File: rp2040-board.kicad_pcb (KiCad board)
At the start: 2 copper layers, 100.9 x 70.3 mm, 20 parts

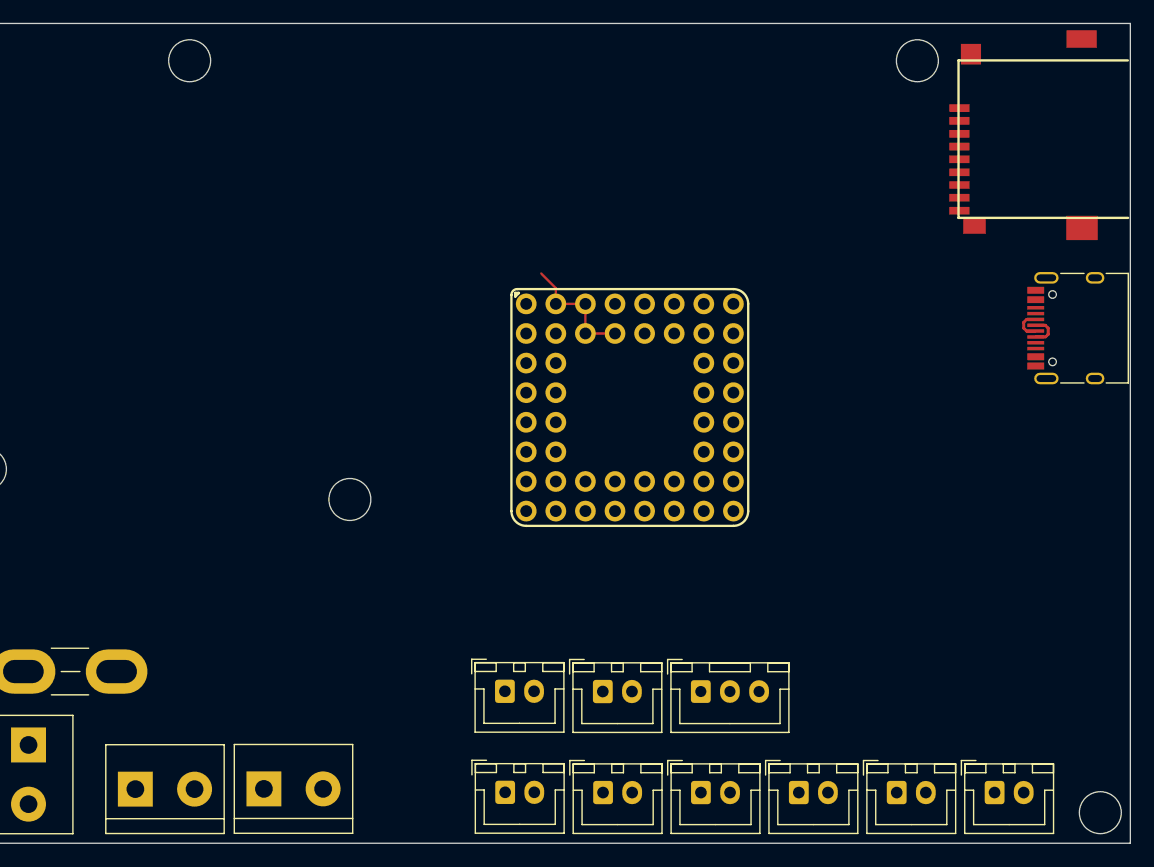
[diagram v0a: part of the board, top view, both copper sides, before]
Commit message: Minor Schematic Layout Changes
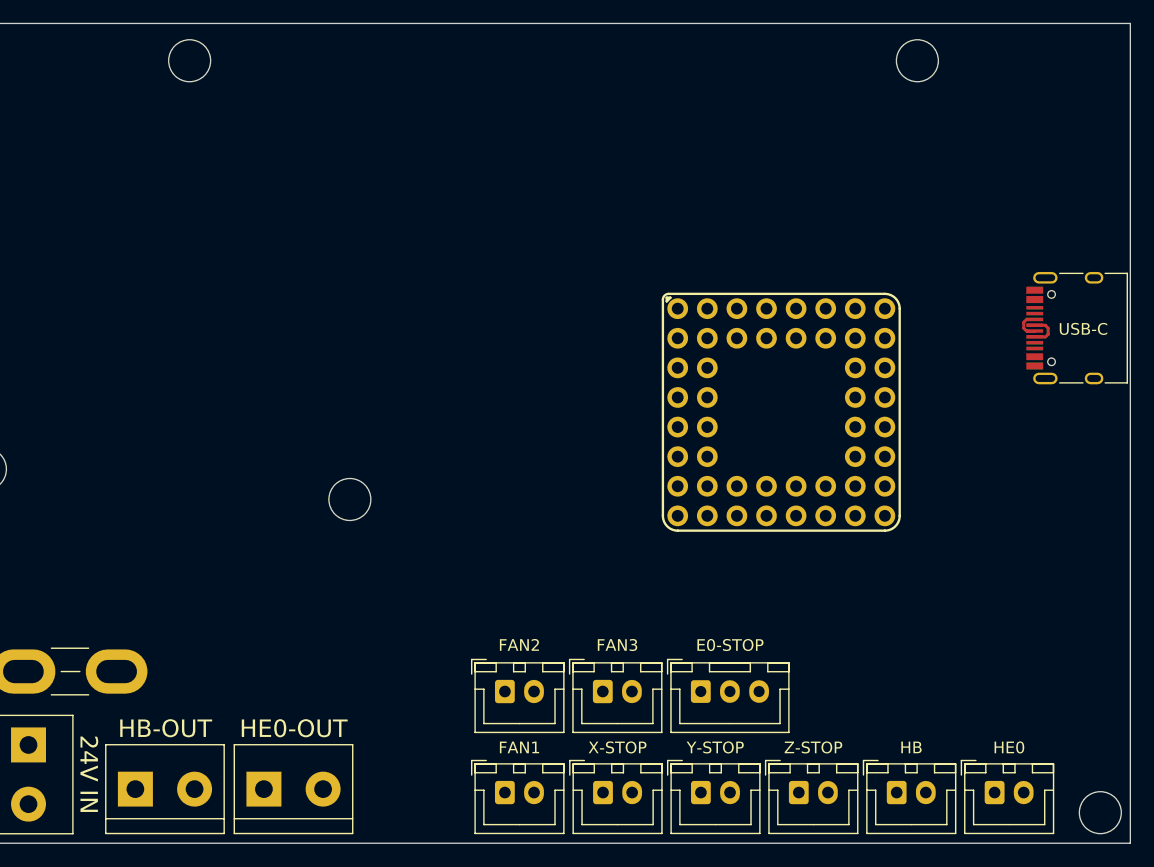
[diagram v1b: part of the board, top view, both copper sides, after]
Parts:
- moved REF** 13.0 mm to (173.0, 101.1)
- moved REF** 0.09 mm to (198.8, 93.9)
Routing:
- net (no net): track 16.4 -> 5.63 mm
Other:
- board text added: "24V IN"
- board text added: "E0-STOP"
- board text added: "FAN1"
- board text added: "FAN2"
- board text added: "FAN3"
- board text added: "HB"
- board text added: "HB-OUT"
- board text added: "HE0"
- board text added: "HE0-OUT"
- board text added: "USB-C"
- board text added: "X-STOP"
- board text added: "Y-STOP"
- board text added: "Z-STOP"

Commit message: Totally no 80% re-source of the BOM
suuurely no re-source
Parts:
- removed the REF** at (198.8, 93.9)
- added C11: 330uF, Capacitor_THT:CP_Radial_D8.0mm_P3.50mm, F.Cu at (109.1, 113.0)
- added C31: 100uF, Capacitor_THT:CP_Radial_D6.3mm_P2.50mm, F.Cu at (121.0, 79.0)
- added C32: 100uF, Capacitor_THT:CP_Radial_D6.3mm_P2.50mm, F.Cu at (141.7, 79.0)
- added C45: 100uF, Capacitor_THT:CP_Radial_D6.3mm_P2.50mm, F.Cu at (162.5, 79.0)
- added C46: 100uF, Capacitor_THT:CP_Radial_D6.3mm_P2.50mm, F.Cu at (183.5, 79.0)
- added J17: X-STEPPER, Connector_JST:JST_XH_B4B-XH-A_1x04_P2.50mm_Vertical, F.Cu at (116.3, 71.9)
- added J18: Y-STEPPER, Connector_JST:JST_XH_B4B-XH-A_1x04_P2.50mm_Vertical, F.Cu at (135.6, 71.9)
- added J19: ZA-STEPPER, Connector_JST:JST_XH_B4B-XH-A_1x04_P2.50mm_Vertical, F.Cu at (150.0, 71.9)
- added J2: USB4105-GF-A, ul_USB4105-GF-A:USB4105-GF-A, F.Cu at (198.8, 93.6)
- added J20: E0-STEPPER, Connector_JST:JST_XH_B4B-XH-A_1x04_P2.50mm_Vertical, F.Cu at (178.8, 71.9)
- added J21: ZB-STEPPER, Connector_JST:JST_XH_B4B-XH-A_1x04_P2.50mm_Vertical, F.Cu at (164.2, 71.9)
- added J5: PROBE, Connector_JST:JST_XH_B5B-XH-A_1x05_P2.50mm_Vertical, F.Cu at (186.0, 124.4)
- F2: renamed from REF**; value Fuse_Blade_Mini_directSolder -> 20A; footprint Fuse:Fuse_Blade_Mini_directSolder -> 01000063Z:01000063Z
- J1: renamed from REF**; value TerminalBlock_bornier-2_P5.08mm -> 24V IN; footprint TerminalBlock:TerminalBlock_bornier-2_P5.08mm -> TerminalBlock_Phoenix:TerminalBlock_Phoenix_MKDS-1,5-2_1x02_P5.00mm_Horizontal
- J10: renamed from REF**; value JST_XH_B3B-XH-A_1x03_P2.50mm_Vertical -> E0-RUNOUT
- J11: renamed from REF**; value JST_XH_B2B-XH-A_1x02_P2.50mm_Vertical -> FAN1
- J12: renamed from REF**; value JST_XH_B2B-XH-A_1x02_P2.50mm_Vertical -> FAN2
- J13: renamed from REF**; value JST_XH_B2B-XH-A_1x02_P2.50mm_Vertical -> FAN3
- J14: renamed from REF**; value TerminalBlock_bornier-2_P5.08mm -> HB; footprint TerminalBlock:TerminalBlock_bornier-2_P5.08mm -> TerminalBlock_Phoenix:TerminalBlock_Phoenix_MKDS-1,5-2_1x02_P5.00mm_Horizontal
- J15: renamed from REF**; value TerminalBlock_bornier-2_P5.08mm -> E0; footprint TerminalBlock:TerminalBlock_bornier-2_P5.08mm -> TerminalBlock_Phoenix:TerminalBlock_Phoenix_MKDS-1,5-2_1x02_P5.00mm_Horizontal
- J16: renamed from REF**; value JST_XH_B2B-XH-A_1x02_P2.50mm_Vertical -> TH-E0
- J3: renamed from REF**; value PGA2040_PTH_NO_SLOT -> PGA2040
- J6: renamed from REF**; value JST_XH_B2B-XH-A_1x02_P2.50mm_Vertical -> X-ENDSTOP
- J7: renamed from REF**; value JST_XH_B2B-XH-A_1x02_P2.50mm_Vertical -> TH-HB
- J8: renamed from REF**; value JST_XH_B2B-XH-A_1x02_P2.50mm_Vertical -> Y-ENDSTOP
- J9: renamed from REF**; value JST_XH_B2B-XH-A_1x02_P2.50mm_Vertical -> Z-ENDSTOP
- moved J10 9.06 mm to (175.1, 124.4)
- moved J12 9.06 mm to (158.3, 124.4)
- moved J13 9.06 mm to (166.7, 124.4)
- moved J3 7.21 mm to (179.9, 103.2)
- moved F2 6.19 mm to (102.0, 121.7)
- moved J1 3.22 mm to (105.2, 129.0)
- moved J14 1.65 mm to (116.3, 132.4)
- moved J15 1.32 mm to (127.8, 132.4)
- moved J11 0.64 mm to (149.9, 133.7)
- moved J16 0.62 mm to (191.9, 133.7)
- moved J6 0.62 mm to (158.3, 133.7)
- moved J7 0.62 mm to (183.5, 133.7)
- moved J8 0.62 mm to (166.7, 133.7)
- moved J9 0.62 mm to (175.1, 133.7)
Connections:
- F2 pad 1: (no net) -> Net-(F2-Pad1)
- F2 pad 2: (no net) -> VCC
- J1 pad 1: (no net) -> Net-(D2-Pad1)
- J1 pad 2: (no net) -> Net-(F2-Pad1)
- J10 pad 1: (no net) -> Net-(C17-Pad1)
- J10 pad 2: (no net) -> GND
- J10 pad 3: (no net) -> +5V
- J11 pad 1: (no net) -> Net-(D7-Pad2)
- J11 pad 2: (no net) -> VCC
- J12 pad 1: (no net) -> Net-(D8-Pad2)
- J12 pad 2: (no net) -> VCC
- J13 pad 1: (no net) -> Net-(D9-Pad2)
- J13 pad 2: (no net) -> VCC
- J14 pad 1: (no net) -> Net-(D10-Pad2)
- J14 pad 2: (no net) -> VCC
- J15 pad 1: (no net) -> Net-(D11-Pad2)
- J15 pad 2: (no net) -> VCC
- J16 pad 1: (no net) -> Net-(J16-Pad1)
- J16 pad 2: (no net) -> GND
- J3 pad A1: (no net) -> GND
- J3 pad A2: (no net) -> +3.3V
- J3 pad A3: (no net) -> +3.3V
- J3 pad A4: (no net) -> Net-(C5-Pad2)
- J3 pad A5: (no net) -> Net-(J2-PadA6)
- J3 pad A6: (no net) -> Net-(J2-PadA7)
- J3 pad A7: (no net) -> Net-(C6-Pad1)
- J3 pad A8: (no net) -> GND
- J3 pad B1: (no net) -> XDIR
- J3 pad B2: (no net) -> GND
- J3 pad B3: (no net) -> +3.3V
- J3 pad B4: (no net) -> +3.3V
- J3 pad B5: (no net) -> unconnected-(J3-PadB5)
- J3 pad B6: (no net) -> unconnected-(J3-PadB6)
- J3 pad B7: (no net) -> GND
- J3 pad B8: (no net) -> /HB_THERM
- J3 pad C1: (no net) -> XSTP
- J3 pad C2: (no net) -> XEN
- J3 pad C7: (no net) -> /E0_THERM
- J3 pad C8: (no net) -> /HB_PWM
- J3 pad D1: (no net) -> /XSTOP
- J3 pad D2: (no net) -> YDIR
- J3 pad D7: (no net) -> /E0_PWM
- J3 pad D8: (no net) -> /FAN3_PWM
- J3 pad E1: (no net) -> YSTP
- J3 pad E2: (no net) -> YEN
- J3 pad E7: (no net) -> /FAN2_PWM
- J3 pad E8: (no net) -> /FAN1_PWM
- J3 pad F1: (no net) -> /YSTOP
- J3 pad F2: (no net) -> ZDIR
- J3 pad F7: (no net) -> Net-(J3-PadF7)
- J3 pad F8: (no net) -> Net-(J3-PadF8)
- J3 pad G1: (no net) -> ZSTP
- J3 pad G2: (no net) -> GND
- J3 pad G3: (no net) -> E0DIR
- J3 pad G4: (no net) -> E0EN
- J3 pad G5: (no net) -> UART_RX
- J3 pad G6: (no net) -> /PROBE_SRVO
- J3 pad G7: (no net) -> GND
- J3 pad G8: (no net) -> Net-(J3-PadG8)
- J3 pad H1: (no net) -> GND
- J3 pad H2: (no net) -> ZEN
- J3 pad H3: (no net) -> /ZSTOP
- J3 pad H4: (no net) -> E0STP
- J3 pad H5: (no net) -> /E0STOP
- J3 pad H6: (no net) -> UART_TX
- J3 pad H7: (no net) -> /PROBE_DET
- J3 pad H8: (no net) -> GND
- J6 pad 1: (no net) -> Net-(C12-Pad1)
- J6 pad 2: (no net) -> GND
- J7 pad 1: (no net) -> Net-(J7-Pad1)
- J7 pad 2: (no net) -> GND
- J8 pad 1: (no net) -> Net-(C15-Pad1)
- J8 pad 2: (no net) -> GND
- J9 pad 1: (no net) -> Net-(C16-Pad1)
- J9 pad 2: (no net) -> GND
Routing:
- net (no net): track 5.63 -> 0.00 mm
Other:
- board size 100.9 x 70.3 mm -> 104 x 70.3 mm
- copper layers 2 -> 4
- board text added: "E0-OUT"
- board text added: "PROBE"
- board text added: "TH-E0"
- board text added: "TH-HB"
- board text added: "X-STEPPER"
- board text added: "Y-STEPPER"
- board text added: "Z-STEPPER"
- board text removed: "HB"
- board text removed: "HE0"
- board text removed: "HE0-OUT"
- board text removed: "USB-C"

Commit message: almost done with layout...
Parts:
- added C1: 10uF, Capacitor_SMD:C_0805_2012Metric_Pad1.18x1.45mm_HandSolder, F.Cu at (109.4, 105.9)
- added C10: 10uF, Capacitor_SMD:C_0805_2012Metric_Pad1.18x1.45mm_HandSolder, F.Cu at (120.0, 105.6)
- added C12: 0.1uF, Capacitor_SMD:C_0805_2012Metric_Pad1.18x1.45mm_HandSolder, F.Cu at (160.7, 127.8)
- added C13: 0.1uF, Capacitor_SMD:C_0805_2012Metric_Pad1.18x1.45mm_HandSolder, F.Cu at (179.3, 125.1)
- added C14: 0.1uF, Capacitor_SMD:C_0805_2012Metric_Pad1.18x1.45mm_HandSolder, F.Cu at (77.5, 41.0)
- added C15: 0.1uF, Capacitor_SMD:C_0805_2012Metric_Pad1.18x1.45mm_HandSolder, F.Cu at (167.6, 127.8)
- added C16: 0.1uF, Capacitor_SMD:C_0805_2012Metric_Pad1.18x1.45mm_HandSolder, F.Cu at (174.7, 127.8)
- added C17: 0.1uF, Capacitor_SMD:C_0805_2012Metric_Pad1.18x1.45mm_HandSolder, F.Cu at (188.4, 115.5)
- added C18: 0.1uF, Capacitor_SMD:C_0805_2012Metric_Pad1.18x1.45mm_HandSolder, F.Cu at (191.8, 125.1)
- added C19: 0.1uF, Capacitor_SMD:C_0805_2012Metric_Pad1.18x1.45mm_HandSolder, F.Cu at (32.4, 41.0)
- added C2: 10uF, Capacitor_SMD:C_0805_2012Metric_Pad1.18x1.45mm_HandSolder, F.Cu at (112.0, 105.9)
- added C20: 0.1uF, Capacitor_SMD:C_0805_2012Metric_Pad1.18x1.45mm_HandSolder, F.Cu at (37.2, 44.0)
- added C21: 0.1uF, Capacitor_SMD:C_0805_2012Metric_Pad1.18x1.45mm_HandSolder, F.Cu at (22.8, 44.0)
- added C22: 22nF, Capacitor_SMD:C_0805_2012Metric_Pad1.18x1.45mm_HandSolder, F.Cu at (22.8, 53.1)
- added C23: 0.1uF, Capacitor_SMD:C_0805_2012Metric_Pad1.18x1.45mm_HandSolder, F.Cu at (27.6, 53.1)
- added C24: 22nF, Capacitor_SMD:C_0805_2012Metric_Pad1.18x1.45mm_HandSolder, F.Cu at (27.6, 41.0)
- added C25: 0.1uF, Capacitor_SMD:C_0805_2012Metric_Pad1.18x1.45mm_HandSolder, F.Cu at (117.4, 77.1)
- added C26: 0.1uF, Capacitor_SMD:C_0805_2012Metric_Pad1.18x1.45mm_HandSolder, F.Cu at (117.4, 81.2)
- added C27: 0.1uF, Capacitor_SMD:C_0805_2012Metric_Pad1.18x1.45mm_HandSolder, F.Cu at (137.9, 77.1)
- added C28: 0.1uF, Capacitor_SMD:C_0805_2012Metric_Pad1.18x1.45mm_HandSolder, F.Cu at (137.9, 81.2)
- added C29: 0.1uF, Capacitor_SMD:C_0805_2012Metric_Pad1.18x1.45mm_HandSolder, F.Cu at (22.8, 47.1)
- added C3: 10uF, Capacitor_SMD:C_0805_2012Metric_Pad1.18x1.45mm_HandSolder, F.Cu at (114.6, 105.9)
- added C30: 0.1uF, Capacitor_SMD:C_0805_2012Metric_Pad1.18x1.45mm_HandSolder, F.Cu at (27.6, 50.1)
- added C33: 0.1uF, Capacitor_SMD:C_0805_2012Metric_Pad1.18x1.45mm_HandSolder, F.Cu at (22.8, 41.0)
- added C34: 0.1uF, Capacitor_SMD:C_0805_2012Metric_Pad1.18x1.45mm_HandSolder, F.Cu at (27.6, 47.1)
- added C35: 0.1uF, Capacitor_SMD:C_0805_2012Metric_Pad1.18x1.45mm_HandSolder, F.Cu at (22.8, 50.1)
- added C36: 22nF, Capacitor_SMD:C_0805_2012Metric_Pad1.18x1.45mm_HandSolder, F.Cu at (22.8, 56.1)
- added C37: 0.1uF, Capacitor_SMD:C_0805_2012Metric_Pad1.18x1.45mm_HandSolder, F.Cu at (27.6, 44.0)
- added C38: 22nF, Capacitor_SMD:C_0805_2012Metric_Pad1.18x1.45mm_HandSolder, F.Cu at (37.2, 41.0)
- added C39: 0.1uF, Capacitor_SMD:C_0805_2012Metric_Pad1.18x1.45mm_HandSolder, F.Cu at (179.5, 77.1)
- added C4: 0.1uF, Capacitor_SMD:C_0805_2012Metric_Pad1.18x1.45mm_HandSolder, F.Cu at (117.2, 105.9)
- added C40: 0.1uF, Capacitor_SMD:C_0805_2012Metric_Pad1.18x1.45mm_HandSolder, F.Cu at (179.5, 81.2)
- added C41: 0.1uF, Capacitor_SMD:C_0805_2012Metric_Pad1.18x1.45mm_HandSolder, F.Cu at (158.7, 77.1)
- added C42: 0.1uF, Capacitor_SMD:C_0805_2012Metric_Pad1.18x1.45mm_HandSolder, F.Cu at (158.7, 81.2)
- added C43: 0.1uF, Capacitor_SMD:C_0805_2012Metric_Pad1.18x1.45mm_HandSolder, F.Cu at (32.4, 44.0)
- added C44: 0.1uF, Capacitor_SMD:C_0805_2012Metric_Pad1.18x1.45mm_HandSolder, F.Cu at (32.4, 47.1)
- added C5: 0.1uF, Capacitor_SMD:C_0805_2012Metric_Pad1.18x1.45mm_HandSolder, F.Cu at (72.7, 44.0)
- added C6: 22uF, Capacitor_SMD:C_0805_2012Metric_Pad1.18x1.45mm_HandSolder, F.Cu at (126.0, 101.4)
- added C7: 0.1uF, Capacitor_SMD:C_0805_2012Metric_Pad1.18x1.45mm_HandSolder, F.Cu at (72.7, 41.0)
- added C8: 0.1uF, Capacitor_SMD:C_0805_2012Metric_Pad1.18x1.45mm_HandSolder, F.Cu at (126.0, 98.2)
- added C9: 0.1uF, Capacitor_SMD:C_0805_2012Metric_Pad1.18x1.45mm_HandSolder, F.Cu at (110.7, 110.3)
- added D1: SS34, Diode_SMD:D_SMA_Handsoldering, F.Cu at (104.3, 111.5)
- added D2: S5BBF, Diode_SMD:D_SMB_Handsoldering, F.Cu at (104.2, 116.3)
- added D3: SS54, Diode_SMD:D_SMA_Handsoldering, F.Cu at (104.3, 100.2)
- added D4: BAV99, BAV99:DIO_BAV99, F.Cu at (183.2, 126.4)
- added D5: BAV99, BAV99:DIO_BAV99, F.Cu at (195.8, 126.5)
- added F1: 0.35A, Fuse:Fuse_1812_4532Metric_Pad1.30x3.40mm_HandSolder, F.Cu at (121.3, 99.6)
- added J4: 3_GPIO, Connector_PinSocket_2.54mm:PinSocket_1x03_P2.54mm_Vertical, F.Cu at (199.7, 111.9)
- added JP1: X-DIAG, Connector_PinHeader_2.54mm:PinHeader_1x02_P2.54mm_Vertical, F.Cu at (123.5, 83.0)
- added JP2: Y-DIAG, Connector_PinHeader_2.54mm:PinHeader_1x02_P2.54mm_Vertical, F.Cu at (144.1, 81.2)
- added JP3: E0-DIAG, Connector_PinHeader_2.54mm:PinHeader_1x02_P2.54mm_Vertical, F.Cu at (185.8, 83.0)
- added JP4: Z-DIAG, Connector_PinHeader_2.54mm:PinHeader_1x02_P2.54mm_Vertical, F.Cu at (164.9, 81.2)
- added L1: 15uH, Inductor_SMD:L_1210_3225Metric_Pad1.42x2.65mm_HandSolder, F.Cu at (115.0, 110.4)
- added Q1: AO3400C, Package_TO_SOT_SMD:SOT-23_Handsoldering, F.Cu at (154.0, 127.2)
- added Q2: AO3400C, Package_TO_SOT_SMD:SOT-23_Handsoldering, F.Cu at (155.9, 120.1)
- added Q3: AO3400C, Package_TO_SOT_SMD:SOT-23_Handsoldering, F.Cu at (174.7, 113.9)
- added R1: 5.1K, Resistor_SMD:R_0805_2012Metric_Pad1.20x1.40mm_HandSolder, F.Cu at (77.5, 44.0)
- added R10: 100R, Resistor_SMD:R_0805_2012Metric_Pad1.20x1.40mm_HandSolder, F.Cu at (157.4, 126.5)
- added R11: 10K, Resistor_SMD:R_0805_2012Metric_Pad1.20x1.40mm_HandSolder, F.Cu at (160.7, 125.1)
- added R12: 2.37K, Resistor_SMD:R_0805_2012Metric_Pad1.20x1.40mm_HandSolder, F.Cu at (179.3, 127.8)
- added R13: 2.37K, Resistor_SMD:R_0805_2012Metric_Pad1.20x1.40mm_HandSolder, F.Cu at (187.2, 127.8)
- added R14: 100R, Resistor_SMD:R_0805_2012Metric_Pad1.20x1.40mm_HandSolder, F.Cu at (185.2, 114.0)
- added R15: 4.7K, Resistor_SMD:R_0805_2012Metric_Pad1.20x1.40mm_HandSolder, F.Cu at (187.2, 125.1)
- added R16: 10R, Resistor_SMD:R_0805_2012Metric_Pad1.20x1.40mm_HandSolder, F.Cu at (117.6, 122.1)
- added R17: 20K, Resistor_SMD:R_0805_2012Metric_Pad1.20x1.40mm_HandSolder, F.Cu at (117.6, 119.4)
- added R18: 10R, Resistor_SMD:R_0805_2012Metric_Pad1.20x1.40mm_HandSolder, F.Cu at (129.6, 119.5)
- added R19: 20K, Resistor_SMD:R_0805_2012Metric_Pad1.20x1.40mm_HandSolder, F.Cu at (129.6, 122.1)
- added R2: 10K, Resistor_SMD:R_0805_2012Metric_Pad1.20x1.40mm_HandSolder, F.Cu at (86.4, 45.8)
- added R20: 10K, Resistor_SMD:R_0805_2012Metric_Pad1.20x1.40mm_HandSolder, F.Cu at (188.4, 112.7)
- added R21: 100R, Resistor_SMD:R_0805_2012Metric_Pad1.20x1.40mm_HandSolder, F.Cu at (164.3, 126.5)
- added R22: 100R, Resistor_SMD:R_0805_2012Metric_Pad1.20x1.40mm_HandSolder, F.Cu at (171.4, 126.5)
- added R23: 10K, Resistor_SMD:R_0805_2012Metric_Pad1.20x1.40mm_HandSolder, F.Cu at (167.6, 125.1)
- added R24: 10K, Resistor_SMD:R_0805_2012Metric_Pad1.20x1.40mm_HandSolder, F.Cu at (174.7, 125.1)
- added R25: 2.37K, Resistor_SMD:R_0805_2012Metric_Pad1.20x1.40mm_HandSolder, F.Cu at (191.8, 127.8)
- added R26: 10R, Resistor_SMD:R_0805_2012Metric_Pad1.20x1.40mm_HandSolder, F.Cu at (149.8, 127.7)
- added R27: 20K, Resistor_SMD:R_0805_2012Metric_Pad1.20x1.40mm_HandSolder, F.Cu at (149.8, 125.0)
- added R28: 10R, Resistor_SMD:R_0805_2012Metric_Pad1.20x1.40mm_HandSolder, F.Cu at (151.7, 120.8)
- added R29: 20K, Resistor_SMD:R_0805_2012Metric_Pad1.20x1.40mm_HandSolder, F.Cu at (151.7, 118.3)
- added R3: 10K, Resistor_SMD:R_0805_2012Metric_Pad1.20x1.40mm_HandSolder, F.Cu at (78.2, 53.5)
- added R30: 10R, Resistor_SMD:R_0805_2012Metric_Pad1.20x1.40mm_HandSolder, F.Cu at (179.2, 113.6)
- added R31: 20K, Resistor_SMD:R_0805_2012Metric_Pad1.20x1.40mm_HandSolder, F.Cu at (179.2, 111.4)
- added R32: 2.37K, Resistor_SMD:R_0805_2012Metric_Pad1.20x1.40mm_HandSolder, F.Cu at (199.7, 127.8)
- added R33: 4.7K, Resistor_SMD:R_0805_2012Metric_Pad1.20x1.40mm_HandSolder, F.Cu at (199.7, 125.1)
- added R34: 100R, Resistor_SMD:R_0805_2012Metric_Pad1.20x1.40mm_HandSolder, F.Cu at (32.4, 53.0)
- added R35: 100R, Resistor_SMD:R_0805_2012Metric_Pad1.20x1.40mm_HandSolder, F.Cu at (41.9, 52.9)
- added R36: 1K, Resistor_SMD:R_0805_2012Metric_Pad1.20x1.40mm_HandSolder, F.Cu at (32.3, 58.9)
- added R37: 20K, Resistor_SMD:R_0805_2012Metric_Pad1.20x1.40mm_HandSolder, F.Cu at (46.7, 41.0)
- added R38: 20K, Resistor_SMD:R_0805_2012Metric_Pad1.20x1.40mm_HandSolder, F.Cu at (41.9, 50.0)
- added R39: 20K, Resistor_SMD:R_0805_2012Metric_Pad1.20x1.40mm_HandSolder, F.Cu at (51.5, 41.0)
- added R4: 10K, Resistor_SMD:R_0805_2012Metric_Pad1.20x1.40mm_HandSolder, F.Cu at (122.7, 105.6)
- added R40: 20K, Resistor_SMD:R_0805_2012Metric_Pad1.20x1.40mm_HandSolder, F.Cu at (41.9, 47.0)
- added R41: 20K, Resistor_SMD:R_0805_2012Metric_Pad1.20x1.40mm_HandSolder, F.Cu at (27.6, 56.1)
- added R42: 20K, Resistor_SMD:R_0805_2012Metric_Pad1.20x1.40mm_HandSolder, F.Cu at (42.0, 44.0)
- added R43: 0.11R, Resistor_SMD:R_0805_2012Metric_Pad1.20x1.40mm_HandSolder, F.Cu at (37.1, 52.9)
- added R44: 0.11R, Resistor_SMD:R_0805_2012Metric_Pad1.20x1.40mm_HandSolder, F.Cu at (37.2, 50.0)
- added R45: 0.11R, Resistor_SMD:R_0805_2012Metric_Pad1.20x1.40mm_HandSolder, F.Cu at (22.8, 59.1)
- added R46: 0.11R, Resistor_SMD:R_0805_2012Metric_Pad1.20x1.40mm_HandSolder, F.Cu at (46.7, 44.0)
- added R47: 20K, Resistor_SMD:R_0805_2012Metric_Pad1.20x1.40mm_HandSolder, F.Cu at (32.4, 50.0)
- added R48: 20K, Resistor_SMD:R_0805_2012Metric_Pad1.20x1.40mm_HandSolder, F.Cu at (42.0, 41.0)
- added R49: 20K, Resistor_SMD:R_0805_2012Metric_Pad1.20x1.40mm_HandSolder, F.Cu at (51.5, 44.0)
- added R5: 3.24K, Resistor_SMD:R_0805_2012Metric_Pad1.20x1.40mm_HandSolder, F.Cu at (125.2, 105.6)
- added R50: 20K, Resistor_SMD:R_0805_2012Metric_Pad1.20x1.40mm_HandSolder, F.Cu at (46.7, 46.9)
- added R51: 20K, Resistor_SMD:R_0805_2012Metric_Pad1.20x1.40mm_HandSolder, F.Cu at (37.1, 58.8)
- added R52: 20K, Resistor_SMD:R_0805_2012Metric_Pad1.20x1.40mm_HandSolder, F.Cu at (37.1, 55.9)
- added R53: 0.11R, Resistor_SMD:R_0805_2012Metric_Pad1.20x1.40mm_HandSolder, F.Cu at (27.6, 59.0)
- added R54: 0.11R, Resistor_SMD:R_0805_2012Metric_Pad1.20x1.40mm_HandSolder, F.Cu at (32.4, 55.9)
- added R55: 0.11R, Resistor_SMD:R_0805_2012Metric_Pad1.20x1.40mm_HandSolder, F.Cu at (46.7, 49.9)
- added R56: 0.11R, Resistor_SMD:R_0805_2012Metric_Pad1.20x1.40mm_HandSolder, F.Cu at (37.2, 47.0)
- added R6: 10K, Resistor_SMD:R_0805_2012Metric_Pad1.20x1.40mm_HandSolder, F.Cu at (78.2, 50.5)
- added R7: 10K, Resistor_SMD:R_0805_2012Metric_Pad1.20x1.40mm_HandSolder, F.Cu at (76.8, 47.0)
- added R8: 10K, Resistor_SMD:R_0805_2012Metric_Pad1.20x1.40mm_HandSolder, F.Cu at (73.5, 51.8)
- added R9: 10K, Resistor_SMD:R_0805_2012Metric_Pad1.20x1.40mm_HandSolder, F.Cu at (73.5, 54.7)
- added RN1: 100R, Resistor_SMD:R_Array_Convex_4x0603, F.Cu at (86.1, 41.9)
- added RN2: 100R, Resistor_SMD:R_Array_Convex_4x0603, F.Cu at (82.0, 41.9)
- added RN3: 100R, Resistor_SMD:R_Array_Convex_4x0603, F.Cu at (72.4, 47.9)
- added RN4: 100R, Resistor_SMD:R_Array_Convex_4x0603, F.Cu at (81.9, 46.7)
- added SW1: SW_MEC_5E, 1825966-1:SW_1825966-1, F.Cu at (66.0, 53.5)
- added U1: AMS1117-3.3, AMS1117-3.3:SOT229P700X180-4N, F.Cu at (114.2, 99.7)
- added U2: TPS5450DDAR, TPS5450:VREG_LM5017MR_NOPB, F.Cu at (113.4, 115.5)
- added U3: 74HCT365D,653, 74HCT365D_653:SOIC127P600X175-16N, F.Cu at (66.1, 45.3)
- added U4: FDS8896, FDS8896:SOIC127P600X175-8N, F.Cu at (123.5, 120.3)
- added U5: FDS8896, FDS8896:SOIC127P600X175-8N, F.Cu at (135.7, 120.3)
- added U6: TMC2226-SA-T, TMC2226:SOP65P640X120-29N, F.Cu at (110.7, 79.1)
- added U7: TMC2226-SA-T, TMC2226:SOP65P640X120-29N, F.Cu at (131.0, 79.1)
- added U8: TMC2226-SA-T, TMC2226:SOP65P640X120-29N, F.Cu at (172.5, 79.1)
- added U9: TMC2226-SA-T, TMC2226:SOP65P640X120-29N, F.Cu at (151.8, 79.1)
- moved J3 21.9 mm to (158.0, 102.3)
- moved C11 13.3 mm to (122.2, 110.6), turned to -90 degrees
- moved J12 5.09 mm to (160.8, 120.0)
- moved J5 5.07 mm to (188.5, 120.0)
- moved J13 5.07 mm to (169.2, 120.0)
- moved J10 5.07 mm to (177.6, 120.0)
- moved C32 3.00 mm to (141.7, 76.0)
- moved C45 3.00 mm to (162.4, 76.0)
- moved J17 2.91 mm to (116.4, 69.0)
- moved J20 2.91 mm to (178.8, 69.0)
- moved J18 2.91 mm to (135.6, 69.0)
- moved J19 2.88 mm to (150.0, 69.0)
- moved J21 2.88 mm to (164.2, 69.0)
- moved J14 1.64 mm to (117.3, 131.1)
- moved J15 1.64 mm to (128.8, 131.1)
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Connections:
- F2 pad 1: Net-(F2-Pad1) -> VCC
- F2 pad 3: (no net) -> Net-(F2-Pad3)
- F2 pad 4: (no net) -> Net-(F2-Pad3)
- J1 pad 1: Net-(D2-Pad1) -> Net-(F2-Pad3)
- J1 pad 2: Net-(F2-Pad1) -> Net-(D2-Pad1)
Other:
- board size 104 x 70.3 mm -> 104 x 75.1 mm
- board text added: "+ -"

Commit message: I am in immense pain
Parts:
- removed SW1: SW_MEC_5E, 1825966-1:SW_1825966-1
- added JP1: RUN, Connector_PinHeader_2.54mm:PinHeader_1x02_P2.54mm_Vertical, F.Cu at (187.1, 102.8)
- moved R1 126.9 mm to (192.7, 97.1), turned to -90 degrees
- moved C5 125.7 mm to (183.8, 102.8), turned to -90 degrees
- moved C7 119.6 mm to (169.6, 111.2)
- moved R2 115.3 mm to (183.8, 107.5), turned to 90 degrees
- moved U3 102.2 mm to (150.3, 103.2)
- moved RN4 99.2 mm to (172.9, 86.0), turned to 90 degrees
- moved C21 97.7 mm to (111.0, 85.8), turned to 90 degrees
- moved R6 96.1 mm to (157.1, 105.5), turned to -90 degrees
- moved C22 94.1 mm to (109.8, 88.8), turned to 180 degrees
- moved C19 93.9 mm to (114.9, 85.8), turned to 90 degrees
- moved C29 93.2 mm to (106.0, 88.8), turned to 180 degrees
- moved R3 91.4 mm to (156.9, 100.0), turned to -90 degrees
- moved C14 91.3 mm to (150.3, 96.2), turned to 180 degrees
- moved R7 88.8 mm to (144.1, 105.1)
- moved RN3 87.9 mm to (151.4, 86.3), turned to 90 degrees
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- renumbered C46 to C45, C45 to C46, JP1 to JP2, JP2 to JP3, JP3 to JP4, JP4 to JP5
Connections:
- net /HEATERS renamed Net-(R26-Pad2)
- C45 pad 2: Net-(C41-Pad1) -> Net-(C39-Pad1)
- C46 pad 2: Net-(C39-Pad1) -> Net-(C41-Pad1)
- F2 pad 1: VCC -> Net-(F2-Pad1)
- F2 pad 2: VCC -> Net-(F2-Pad1)
- F2 pad 3: Net-(F2-Pad3) -> VCC
- F2 pad 4: Net-(F2-Pad3) -> VCC
- J1 pad 1: Net-(F2-Pad3) -> Net-(F2-Pad1)
- J14 pad 1: Net-(J14-Pad1) -> VCC
- J14 pad 2: VCC -> Net-(J14-Pad2)
- J15 pad 1: Net-(J15-Pad1) -> VCC
- J15 pad 2: VCC -> Net-(J15-Pad2)
- J3 pad D1: /XSTOP -> XSTOP
- J3 pad F1: /YSTOP -> YSTOP
- J3 pad H3: /ZSTOP -> ZSTOP
- J3 pad H5: /E0STOP -> E0STOP
- R10 pad 2: /XSTOP -> XSTOP
- R14 pad 2: /E0STOP -> E0STOP
- R21 pad 2: /YSTOP -> YSTOP
- R22 pad 2: /ZSTOP -> ZSTOP
- U4 pad 5: Net-(J14-Pad1) -> Net-(J14-Pad2)
- U4 pad 6: Net-(J14-Pad1) -> Net-(J14-Pad2)
- U4 pad 7: Net-(J14-Pad1) -> Net-(J14-Pad2)
- U4 pad 8: Net-(J14-Pad1) -> Net-(J14-Pad2)
- U5 pad 5: Net-(J15-Pad1) -> Net-(J15-Pad2)
- U5 pad 6: Net-(J15-Pad1) -> Net-(J15-Pad2)
- U5 pad 7: Net-(J15-Pad1) -> Net-(J15-Pad2)
- U5 pad 8: Net-(J15-Pad1) -> Net-(J15-Pad2)
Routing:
- net GND: track 0.00 -> 290.2 mm, vias 0 -> 40
- net +3.3V: track 0.00 -> 199.2 mm, vias 0 -> 9
- net VCC: track 0.00 -> 135.4 mm, vias 0 -> 3
- net +5V: track 0.00 -> 60.7 mm, vias 0 -> 3
- net /PROBE_DET: track 0.00 -> 47.6 mm
- net Net-(R30-Pad2): track 0.00 -> 39.9 mm, vias 0 -> 2
- net /PROBE_SRVO: track 0.00 -> 39.5 mm
- net Net-(C1-Pad1): track 0.00 -> 30.0 mm, vias 0 -> 3
- net Net-(R26-Pad2): track 0.00 -> 28.7 mm, vias 0 -> 2
- net Net-(R4-Pad2): track 0.00 -> 26.4 mm, vias 0 -> 2
- net Net-(C5-Pad2): track 0.00 -> 25.3 mm, vias 0 -> 1
- net Net-(C9-Pad2): track 0.00 -> 24.5 mm
- net /FAN2_PWM: track 0.00 -> 23.7 mm, vias 0 -> 1
- net Net-(D2-Pad1): track 0.00 -> 23.6 mm
- net XDIR: track 0.00 -> 21.2 mm, vias 0 -> 2
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- added copper zone on In1.Cu, net GND
- added copper zone on F.Cu, net Net-(D2-Pad1)
- added copper zone on F.Cu, net Net-(F2-Pad1)
- added copper zone on F.Cu, net Net-(J14-Pad2)
- added copper zone on F.Cu, net Net-(J15-Pad2)
- added copper zone on F.Cu, net VCC
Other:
- board size 104 x 75.1 mm -> 105.3 x 75.1 mm

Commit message: idk
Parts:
- turned R38 to 90 degrees
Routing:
- net XEN: track 2.81 -> 12.5 mm, vias 0 -> 2
- net GND: track 290.2 -> 286.6 mm
- net Net-(R35-Pad1): track 0.00 -> 1.69 mm, vias 0 -> 1
- net VCC: track 135.4 -> 136.6 mm
- net Net-(C29-Pad1): track 14.9 -> 14.0 mm
- net Net-(R38-Pad1): track 0.00 -> 0.84 mm, vias 0 -> 1
- net Net-(C22-Pad1): track 9.58 -> 8.86 mm
- net Net-(C22-Pad2): track 10.1 -> 9.43 mm

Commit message: so very close to done
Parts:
- moved C33 172.5 mm to (189.4, 85.8), turned to 90 degrees
- moved C35 168.5 mm to (187.4, 85.8), turned to 90 degrees
- moved C36 162.5 mm to (182.5, 85.9), turned to 180 degrees
- moved C43 158.6 mm to (185.4, 85.8), turned to -90 degrees
- moved R53 151.4 mm to (177.5, 80.1), turned to 180 degrees
- moved R47 147.8 mm to (177.5, 78.2), turned to 180 degrees
- moved R54 147.5 mm to (177.5, 82.0)
- moved R51 145.1 mm to (179.7, 85.8), turned to 90 degrees
- moved C34 142.3 mm to (164.5, 85.8), turned to 90 degrees
- moved C37 141.2 mm to (162.5, 85.8), turned to 90 degrees
- moved R48 140.0 mm to (177.5, 76.2), turned to 180 degrees
- moved R34 134.5 mm to (159.5, 97.0)
- moved C44 133.8 mm to (160.5, 85.8), turned to -90 degrees
- moved R36 128.7 mm to (155.2, 97.0)
- moved C38 128.5 mm to (157.6, 85.9), turned to 180 degrees
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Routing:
- net VCC: track 136.6 -> 225.9 mm, vias 3 -> 9
- net Net-(R35-Pad1): track 1.69 -> 60.1 mm, vias 1 -> 8
- net Net-(J19-Pad3): track 0.00 -> 34.5 mm, vias 0 -> 1
- net ZDIR: track 0.00 -> 27.0 mm, vias 0 -> 2
- net ZSTP: track 0.00 -> 23.0 mm, vias 0 -> 2
- net YDIR: track 0.00 -> 20.9 mm, vias 0 -> 2
- net E0DIR: track 0.00 -> 20.9 mm, vias 0 -> 2
- net E0EN: track 0.00 -> 20.0 mm, vias 0 -> 2
- net YEN: track 0.00 -> 20.0 mm, vias 0 -> 2
- net Net-(J20-Pad4): track 0.00 -> 20.0 mm
- net Net-(J18-Pad4): track 0.00 -> 19.2 mm
- net E0STP: track 0.00 -> 17.9 mm, vias 0 -> 2
- net YSTP: track 0.00 -> 17.9 mm, vias 0 -> 2
- net Net-(R50-Pad1): track 0.00 -> 16.2 mm, vias 0 -> 2
- net Net-(R48-Pad1): track 0.00 -> 16.2 mm, vias 0 -> 2
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- added copper zone on F.Cu, net +3.3V

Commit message: soooooooo close
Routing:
- net +3.3V: track 210.5 -> 298.9 mm
- net Net-(R16-Pad2): track 2.70 -> 44.2 mm, vias 0 -> 2
- net Net-(R18-Pad2): track 2.60 -> 33.8 mm, vias 0 -> 2
- net Net-(J19-Pad4): track 0.00 -> 20.0 mm
- net Net-(J19-Pad3): track 34.5 -> 14.6 mm
